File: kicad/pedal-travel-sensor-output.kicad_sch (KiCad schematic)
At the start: 20 parts, among them U10 VOMA617A-8X001T, U5 VOMA617A-8X001T, U6 VOMA617A-8X001T, U7 VOMA617A-8X001T, U8 VOMA617A-8X001T, U9 VOMA617A-8X001T

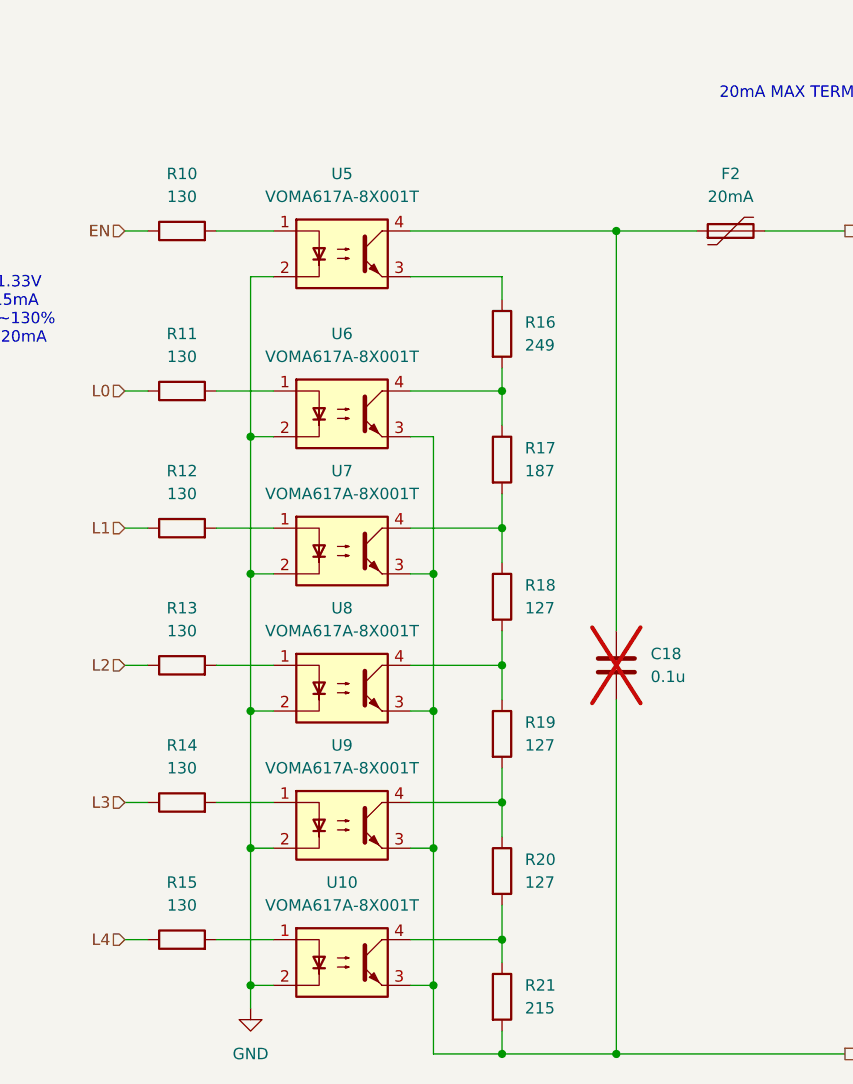
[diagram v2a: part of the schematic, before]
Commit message: Add optional RC filter to pressure sensor inputs
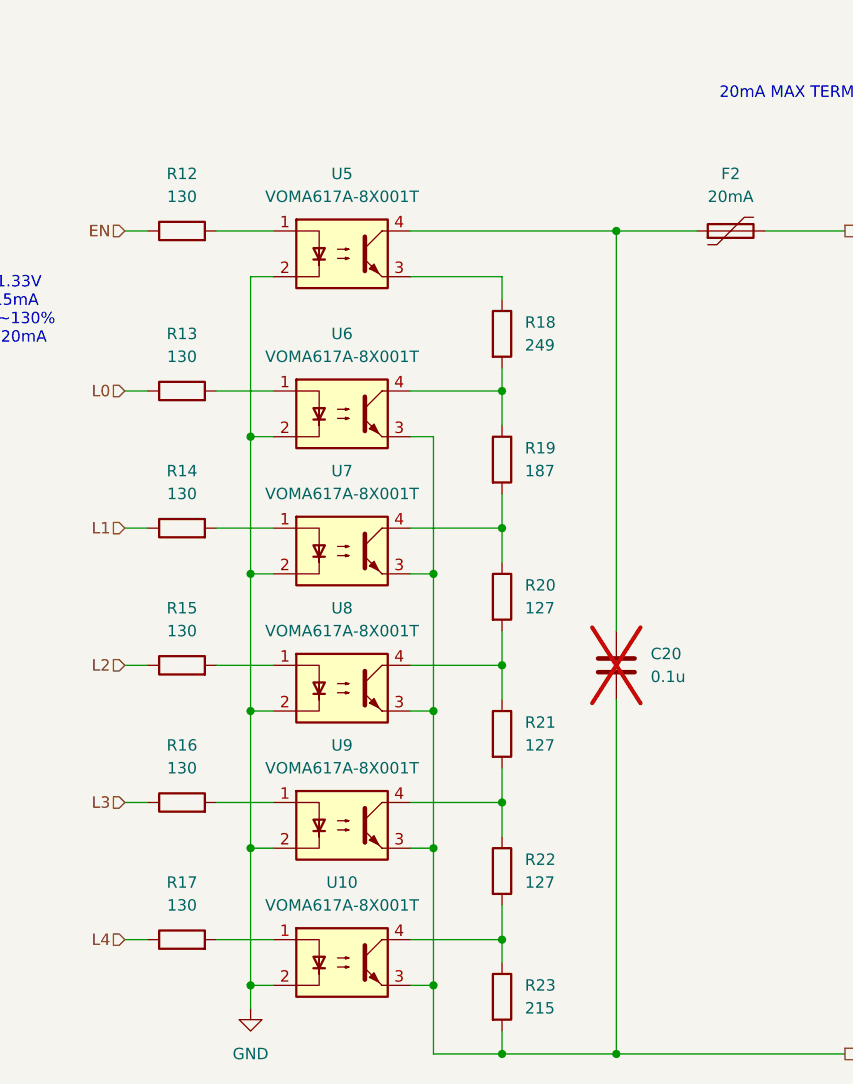
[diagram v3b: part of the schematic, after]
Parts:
- renumbered C18 to C20, R10 to R12, R11 to R13, R12 to R14, R13 to R15, R14 to R16, R15 to R17, R16 to R18, R17 to R19, R18 to R20, R19 to R21, R20 to R22, R21 to R23
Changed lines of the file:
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@@
 		(dnp no)
 		(fields_autoplaced yes)
-		(property "Reference" "#PWR036"
+		(property "Reference" "#PWR038"
 			(at 149.86 179.07 0)
 			(hide yes)
@@
 			(project "bmw-e36-abs-adapter"
 				(path "/325be93f-b4a6-4f2b-83c3-2ccd33e5cc03/3e268bd5-2ae2-4112-b445-da0f11812250"
-					(reference "#PWR036")
+					(reference "#PWR038")
 					(unit 1)
 				)
@@
 		(dnp no)
 		(fields_autoplaced yes)
-		(property "Reference" "R21"
+		(property "Reference" "R23"
 			(at 180.34 170.1799 0)
 			(show_name no)
@@
 			(project "bmw-e36-abs-adapter"
 				(path "/325be93f-b4a6-4f2b-83c3-2ccd33e5cc03/3e268bd5-2ae2-4112-b445-da0f11812250"
-					(reference "R21")
+					(reference "R23")
 					(unit 1)
 				)
@@
 		(dnp no)
 		(fields_autoplaced yes)
-		(property "Reference" "R17"
+		(property "Reference" "R19"
 			(at 180.34 110.4899 0)
 			(show_name no)
@@
 			(project "bmw-e36-abs-adapter"
 				(path "/325be93f-b4a6-4f2b-83c3-2ccd33e5cc03/3e268bd5-2ae2-4112-b445-da0f11812250"
-					(reference "R17")
+					(reference "R19")
 					(unit 1)
 				)
@@
 		(dnp no)
 		(fields_autoplaced yes)
-		(property "Reference" "R11"
+		(property "Reference" "R13"
 			(at 142.24 97.79 90)
 			(show_name no)
@@
 			(project "bmw-e36-abs-adapter"
 				(path "/325be93f-b4a6-4f2b-83c3-2ccd33e5cc03/3e268bd5-2ae2-4112-b445-da0f11812250"
-					(reference "R11")
+					(reference "R13")
 					(unit 1)
 				)
@@
 		(dnp no)
 		(fields_autoplaced yes)
-		(property "Reference" "R18"
+		(property "Reference" "R20"
 			(at 180.34 125.7299 0)
 			(show_name no)
@@
 			(project "bmw-e36-abs-adapter"
 				(path "/325be93f-b4a6-4f2b-83c3-2ccd33e5cc03/3e268bd5-2ae2-4112-b445-da0f11812250"
-					(reference "R18")
+					(reference "R20")
 					(unit 1)
 				)
@@
 		(dnp no)
 		(fields_autoplaced yes)
-		(property "Reference" "R19"
+		(property "Reference" "R21"
 			(at 180.34 140.9699 0)
 			(show_name no)
@@
 			(project "bmw-e36-abs-adapter"
 				(path "/325be93f-b4a6-4f2b-83c3-2ccd33e5cc03/3e268bd5-2ae2-4112-b445-da0f11812250"
-					(reference "R19")
+					(reference "R21")
 					(unit 1)
 				)
@@
 		(dnp no)
 		(fields_autoplaced yes)
-		(property "Reference" "R16"
+		(property "Reference" "R18"
 			(at 180.34 96.5199 0)
 			(show_name no)
@@
 			(project "bmw-e36-abs-adapter"
 				(path "/325be93f-b4a6-4f2b-83c3-2ccd33e5cc03/3e268bd5-2ae2-4112-b445-da0f11812250"
-					(reference "R16")
+					(reference "R18")
 					(unit 1)
 				)
@@
 		(dnp no)
 		(fields_autoplaced yes)
-		(property "Reference" "R14"
+		(property "Reference" "R16"
 			(at 142.24 143.51 90)
 			(show_name no)
@@
 			(project "bmw-e36-abs-adapter"
 				(path "/325be93f-b4a6-4f2b-83c3-2ccd33e5cc03/3e268bd5-2ae2-4112-b445-da0f11812250"
-					(reference "R14")
+					(reference "R16")
 					(unit 1)
 				)
@@
 		(dnp no)
 		(fields_autoplaced yes)
-		(property "Reference" "R13"
+		(property "Reference" "R15"
 			(at 142.24 128.27 90)
 			(show_name no)
@@
 			(project "bmw-e36-abs-adapter"
 				(path "/325be93f-b4a6-4f2b-83c3-2ccd33e5cc03/3e268bd5-2ae2-4112-b445-da0f11812250"
-					(reference "R13")
+					(reference "R15")
 					(unit 1)
 				)
@@
 		(dnp no)
 		(fields_autoplaced yes)
-		(property "Reference" "R20"
+		(property "Reference" "R22"
 			(at 180.34 156.2099 0)
 			(show_name no)
@@
 			(project "bmw-e36-abs-adapter"
 				(path "/325be93f-b4a6-4f2b-83c3-2ccd33e5cc03/3e268bd5-2ae2-4112-b445-da0f11812250"
-					(reference "R20")
+					(reference "R22")
 					(unit 1)
 				)
@@
 		(dnp no)
 		(fields_autoplaced yes)
-		(property "Reference" "R12"
+		(property "Reference" "R14"
 			(at 142.24 113.03 90)
 			(show_name no)
@@
 			(project "bmw-e36-abs-adapter"
 				(path "/325be93f-b4a6-4f2b-83c3-2ccd33e5cc03/3e268bd5-2ae2-4112-b445-da0f11812250"
-					(reference "R12")
+					(reference "R14")
 					(unit 1)
 				)
@@
 		(dnp no)
 		(fields_autoplaced yes)
-		(property "Reference" "R15"
+		(property "Reference" "R17"
 			(at 142.24 158.75 90)
 			(show_name no)
@@
 			(project "bmw-e36-abs-adapter"
 				(path "/325be93f-b4a6-4f2b-83c3-2ccd33e5cc03/3e268bd5-2ae2-4112-b445-da0f11812250"
-					(reference "R15")
+					(reference "R17")
 					(unit 1)
 				)
@@
 		(dnp yes)
 		(fields_autoplaced yes)
-		(property "Reference" "C18"
+		(property "Reference" "C20"
 			(at 194.31 133.3499 0)
 			(show_name no)
@@
 			(project "bmw-e36-abs-adapter"
 				(path "/325be93f-b4a6-4f2b-83c3-2ccd33e5cc03/3e268bd5-2ae2-4112-b445-da0f11812250"
-					(reference "C18")
+					(reference "C20")
 					(unit 1)
 				)
@@
 		(dnp no)
 		(fields_autoplaced yes)
-		(property "Reference" "R10"
+		(property "Reference" "R12"
 			(at 142.24 80.01 90)
 			(show_name no)
@@
 			(project "bmw-e36-abs-adapter"
 				(path "/325be93f-b4a6-4f2b-83c3-2ccd33e5cc03/3e268bd5-2ae2-4112-b445-da0f11812250"
-					(reference "R10")
-					(unit 1)
-				)
+					(reference "R12")
+					(unit 1)
+				)

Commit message: Update footprints
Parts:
- U10, U5, U6, U7, U8, U9: footprint (none) -> bmw-e36-abs-adapter:SOP-4_4.4x4.6mm_P2.54mm
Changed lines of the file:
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@@
 			)
 		)
-		(property "Footprint" ""
+		(property "Footprint" "bmw-e36-abs-adapter:SOP-4_4.4x4.6mm_P2.54mm"
 			(at 154.94 93.98 0)
 			(hide yes)
@@
 			)
 		)
-		(property "Footprint" ""
+		(property "Footprint" "bmw-e36-abs-adapter:SOP-4_4.4x4.6mm_P2.54mm"
 			(at 154.94 172.72 0)
 			(hide yes)
@@
 			)
 		)
-		(property "Footprint" ""
+		(property "Footprint" "bmw-e36-abs-adapter:SOP-4_4.4x4.6mm_P2.54mm"
 			(at 154.94 127 0)
 			(hide yes)
@@
 			)
 		)
-		(property "Footprint" ""
+		(property "Footprint" "bmw-e36-abs-adapter:SOP-4_4.4x4.6mm_P2.54mm"
 			(at 154.94 157.48 0)
 			(hide yes)
@@
 			)
 		)
-		(property "Footprint" ""
+		(property "Footprint" "bmw-e36-abs-adapter:SOP-4_4.4x4.6mm_P2.54mm"
 			(at 154.94 111.76 0)
 			(hide yes)
@@
 			)
 		)
-		(property "Footprint" ""
+		(property "Footprint" "bmw-e36-abs-adapter:SOP-4_4.4x4.6mm_P2.54mm"
 			(at 154.94 142.24 0)
 			(hide yes)

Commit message: Update part numbers and fix ERC issues
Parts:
- C20: Manufacturer (none) -> Murata; Part Number (none) -> GCJ188R71H104KA12D; now left out of the parts list
- R12, R13, R14, R15, R16, R17: Manufacturer (none) -> Panasonic; Part Number (none) -> ERJ-3EKF1300V
- R18: Manufacturer (none) -> Panasonic; Part Number (none) -> ERJ-3EKF2490V
- R19: Manufacturer (none) -> Panasonic; Part Number (none) -> ERJ-3EKF1870V
- R20, R21, R22: Manufacturer (none) -> Panasonic; Part Number (none) -> ERJ-3EKF1270V
- R23: Manufacturer (none) -> Panasonic; Part Number (none) -> ERJ-3EKF2150V
